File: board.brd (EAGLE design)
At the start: 70 x 70 mm, 6 parts

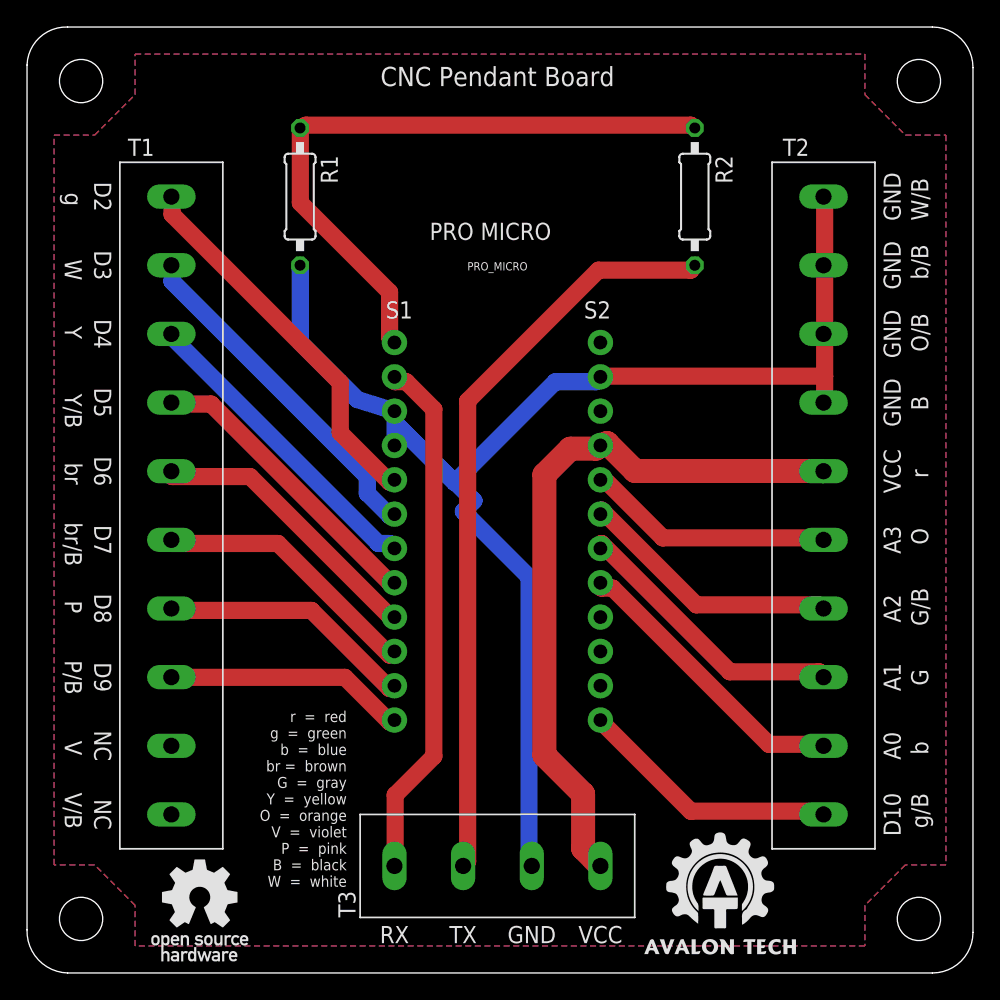
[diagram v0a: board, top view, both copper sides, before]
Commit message: update for jlcpcb pcba
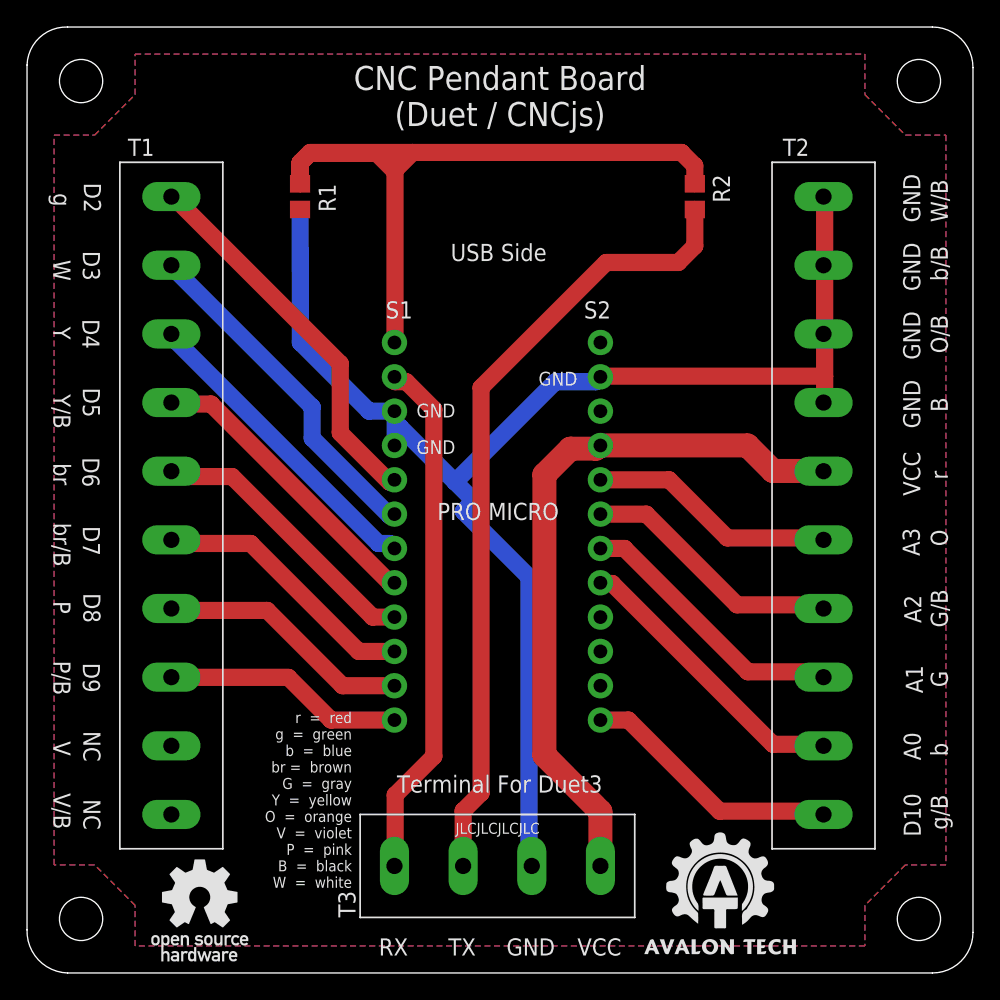
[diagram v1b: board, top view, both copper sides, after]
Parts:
- R1, R2: device rcl:0207/10 -> rcl:R0805
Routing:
- net N$16: track 48.1 -> 56.9 mm
- net GND: track 101.6 -> 106.0 mm
- net N$18: track 55.5 -> 58.8 mm
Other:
- board text added: "JLCJLCJLCJLC"
- board text added: "Terminal For Duet3"
- board text added: "USB Side"
- board text removed: "CNC Pendant Board"
